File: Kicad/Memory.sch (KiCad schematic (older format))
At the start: 7 parts, among them U1 74HCT238, U2 74HCT574, U3 CY62148, U4 AT28C64B

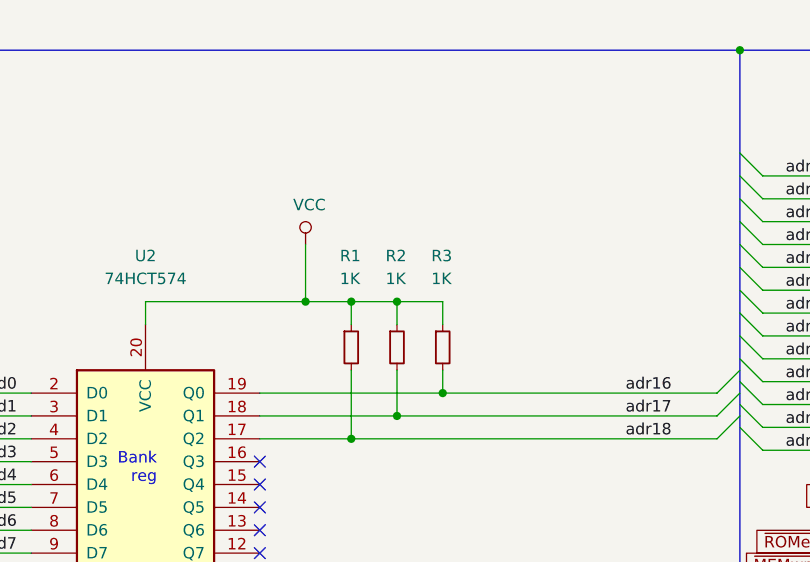
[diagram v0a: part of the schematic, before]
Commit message: The PCB design is done, schematic updated, PCBs ordered.
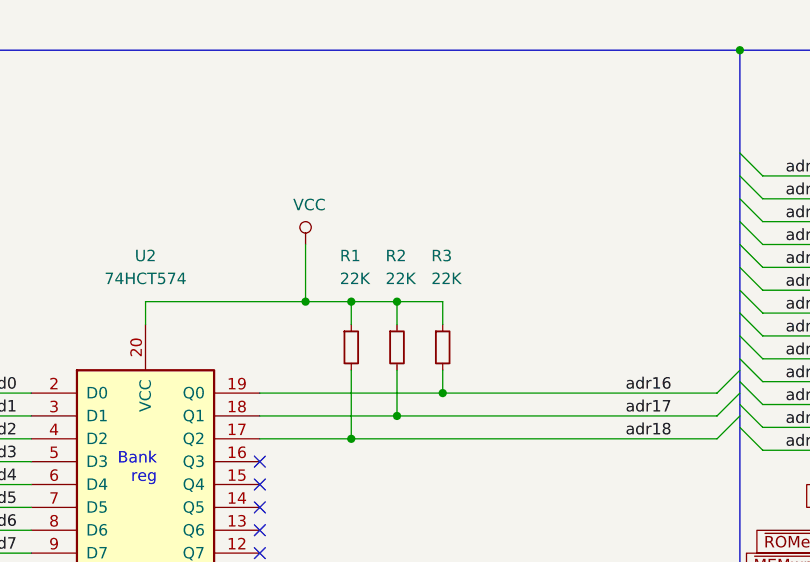
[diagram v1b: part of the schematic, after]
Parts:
- R1, R2, R3: value 1K -> 22K
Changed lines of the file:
@@
 P 5950 2200
 F 0 "R1" H 5900 2600 50  0000 L CNN
-F 1 "1K" H 5900 2500 50  0000 L CNN
+F 1 "22K" H 5900 2500 50  0000 L CNN
 F 2 "Resistor_SMD:R_0603_1608Metric_Pad1.05x0.95mm_HandSolder" H 5950 2200 50  0001 C CNN
 F 3 "~" H 5950 2200 50  0001 C CNN
@@
 P 6150 2200
 F 0 "R2" H 6100 2600 50  0000 L CNN
-F 1 "1K" H 6100 2500 50  0000 L CNN
+F 1 "22K" H 6100 2500 50  0000 L CNN
 F 2 "Resistor_SMD:R_0603_1608Metric_Pad1.05x0.95mm_HandSolder" H 6150 2200 50  0001 C CNN
 F 3 "~" H 6150 2200 50  0001 C CNN
@@
 P 6350 2200
 F 0 "R3" H 6300 2600 50  0000 L CNN
-F 1 "1K" H 6300 2500 50  0000 L CNN
+F 1 "22K" H 6300 2500 50  0000 L CNN
 F 2 "Resistor_SMD:R_0603_1608Metric_Pad1.05x0.95mm_HandSolder" H 6350 2200 50  0001 C CNN
 F 3 "~" H 6350 2200 50  0001 C CNN
